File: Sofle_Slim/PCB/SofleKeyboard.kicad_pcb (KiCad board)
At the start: 2 copper layers, 143.4 x 111.8 mm, 84 parts, among them J2 4PIN, J3 OLED, P1 i2c_pin, P2 i2c_pin, SW1 SW_PUSH_LED, SW10 SW_PUSH_LED, SW11 SW_PUSH_LED, SW12 SW_PUSH_LED, SW13 SW_PUSH_LED, SW14 SW_PUSH_LED, SW15 SW_PUSH_LED, SW16 SW_PUSH_LED, SW17 SW_PUSH_LED, SW18 SW_PUSH_LED, SW19 SW_PUSH_LED, SW2 SW_PUSH_LED, SW20 SW_PUSH_LED, SW21 SW_PUSH_LED, SW22 SW_PUSH_LED, SW23 SW_PUSH_LED, SW24 SW_PUSH_LED, SW25 Rotary_Encoder_Switch, SW26 SW_PUSH_LED, SW27 SW_PUSH_LED, SW28 SW_PUSH_LED, SW29 SW_PUSH_LED, SW3 SW_PUSH_LED, SW30 SW_PUSH_LED, SW4 SW_PUSH_LED, SW5 SW_PUSH_LED, SW6 SW_PUSH_LED, SW7 SW_PUSH_LED, SW8 SW_PUSH_LED, SW9 SW_PUSH_LED, U1 ProMicro

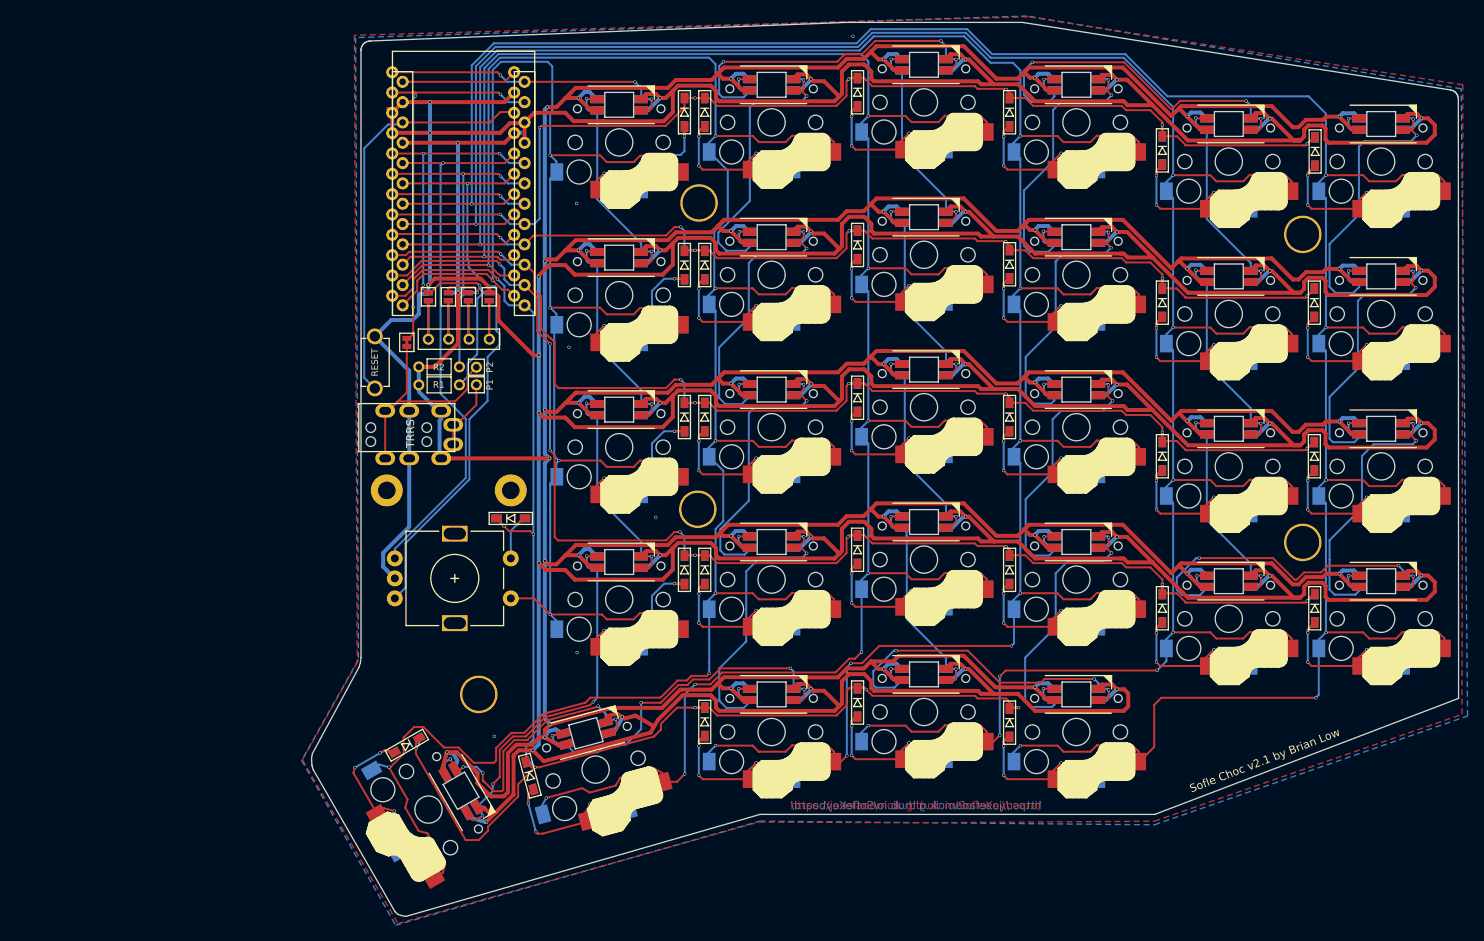
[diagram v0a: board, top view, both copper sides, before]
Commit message: changed usb-c plug for usb receptacle
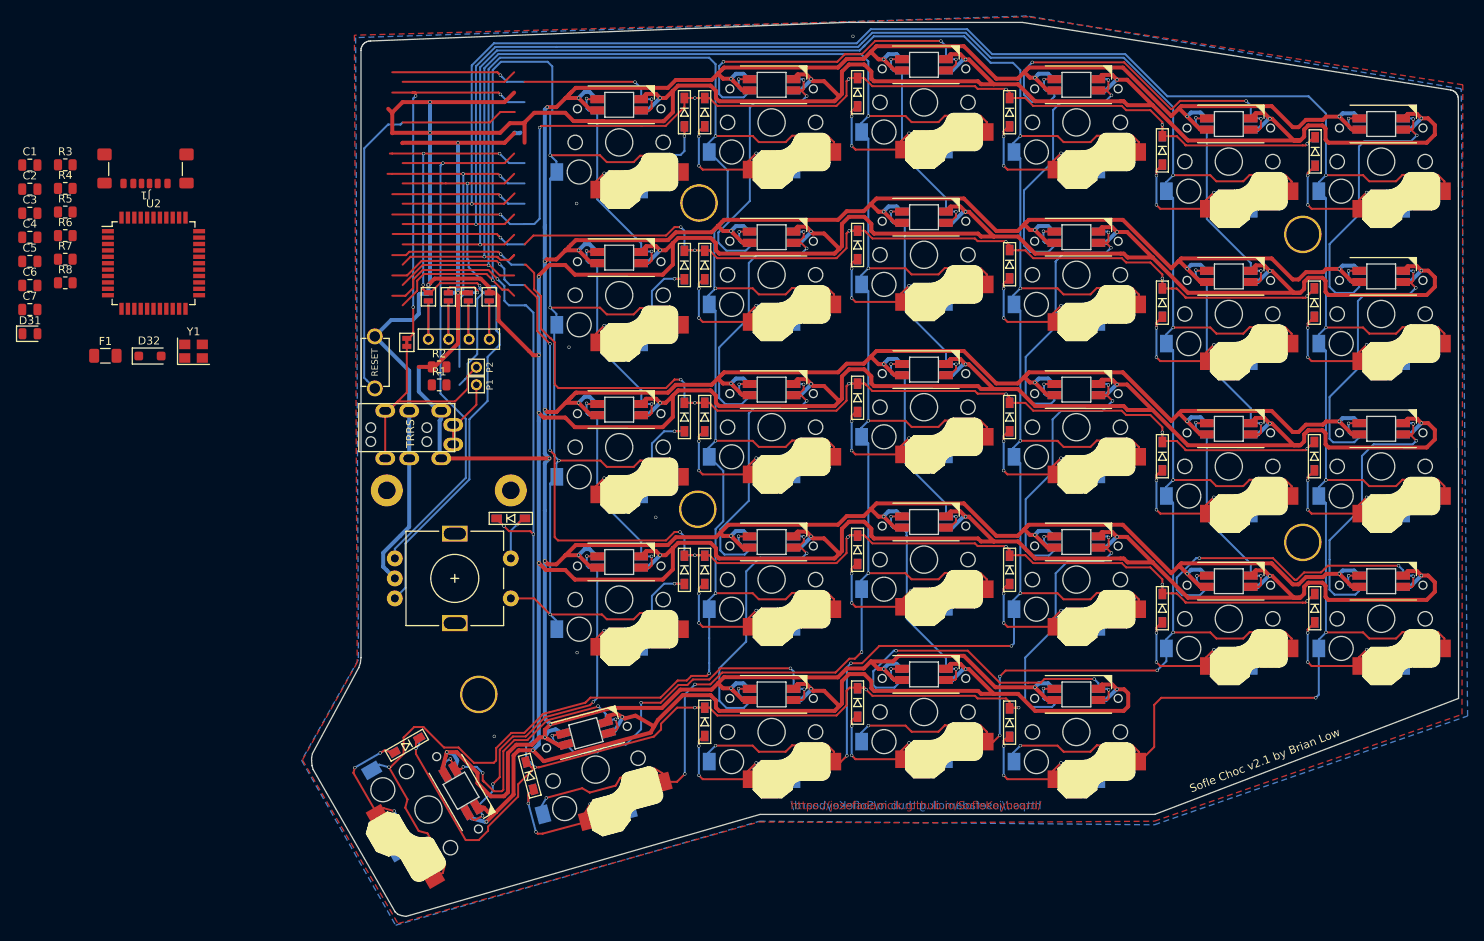
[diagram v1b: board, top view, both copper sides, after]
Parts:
- removed U1: ProMicro, SofleKeyboard-footprint:ProMicro
- added C1: 0.1uF, Capacitor_SMD:C_0805_2012Metric, F.Cu at (46.9, 52.8)
- added C2: 0.1uF, Capacitor_SMD:C_0805_2012Metric, F.Cu at (46.9, 55.8)
- added C3: 0.1uF, Capacitor_SMD:C_0805_2012Metric, F.Cu at (46.9, 58.9)
- added C4: 10uF, Capacitor_SMD:C_0805_2012Metric, F.Cu at (46.9, 61.9)
- added C5: 22pF, Capacitor_SMD:C_0805_2012Metric, F.Cu at (46.9, 64.9)
- added C6: 22pF, Capacitor_SMD:C_0805_2012Metric, F.Cu at (46.9, 67.9)
- added C7: 1uF, Capacitor_SMD:C_0805_2012Metric, F.Cu at (46.9, 70.9)
- added D31: PWR_LED, LED_SMD:LED_0805_2012Metric, F.Cu at (46.9, 73.9)
- added D32: D_Schottky, Diode_SMD:D_SOD-123F, F.Cu at (61.9, 76.7)
- added F1: 500mA, Fuse:Fuse_1206_3216Metric, F.Cu at (56.3, 76.7)
- added J1: USB_C_Receptacle_USB2.0_14P, Connector_USB:USB_C_Receptacle_GCT_USB4135-GF-A_6P_TopMnt_Horizontal, F.Cu at (61.3, 52.1)
- added R3: R_LED, Resistor_SMD:R_0805_2012Metric, F.Cu at (51.3, 52.8)
- added R4: 5.1K, Resistor_SMD:R_0805_2012Metric, F.Cu at (51.3, 55.8)
- added R5: 5.1K, Resistor_SMD:R_0805_2012Metric, F.Cu at (51.3, 58.7)
- added R6: 22, Resistor_SMD:R_0805_2012Metric, F.Cu at (51.3, 61.7)
- added R7: 22, Resistor_SMD:R_0805_2012Metric, F.Cu at (51.3, 64.6)
- added R8: 10k, Resistor_SMD:R_0805_2012Metric, F.Cu at (51.3, 67.6)
- added U2: ATmega32U4-A, Package_QFP:TQFP-44_10x10mm_P0.8mm, F.Cu at (62.3, 65.1)
- added Y1: 16MHz, Crystal:Crystal_SMD_3225-4Pin_3.2x2.5mm, F.Cu at (67.3, 76.1)
- R1, R2: footprint SofleKeyboard-footprint:RESISTOR_mini -> Resistor_SMD:R_0805_2012Metric
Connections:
- J2 pad 1: VCC -> +5V
- JP2 pad 2: VCC -> +5V
- JP7 pad 2: VCC -> +5V
- R1 pad 1: VCC -> +5V
- R2 pad 1: VCC -> +5V
- SW6 pad 2: Net-(SW6-Pad2) -> unconnected-(SW6B-DOUT-Pad2)
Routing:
- net +5V: track 0.00 -> 48.4 mm, vias 0 -> 2
- net VCC: track 889.9 -> 841.6 mm, vias 37 -> 35
- net GND: track 1090.4 -> 1121.9 mm, vias 43 -> 44
- net Net-(U1-Pad7): track 17.0 -> 0.00 mm, vias 1 -> 0
- net LED: track 37.3 -> 20.3 mm, vias 3 -> 2
- net (no net): track 0.00 -> 17.0 mm, vias 0 -> 1
- net Net-(U1-Pad24): track 14.4 -> 0.00 mm
- net unconnected-(SW6B-DOUT-Pad2): track 0.00 -> 3.91 mm, vias 0 -> 1
- net Net-(SW6-Pad2): track 3.91 -> 0.00 mm, vias 1 -> 0
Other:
- net class Default removed
- net class GND removed
- net class VCC removed
